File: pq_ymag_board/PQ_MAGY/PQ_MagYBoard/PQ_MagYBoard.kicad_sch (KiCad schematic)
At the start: 10 parts, among them J1 M20-7810245

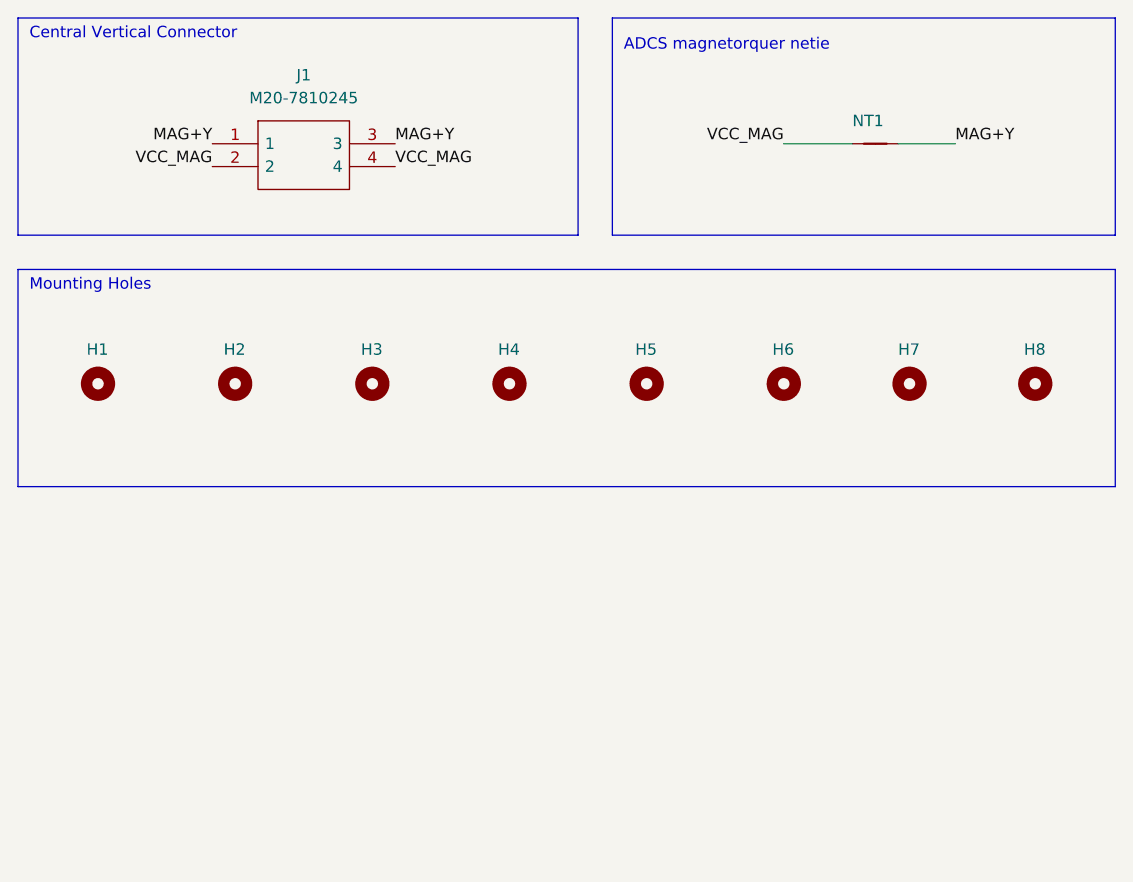
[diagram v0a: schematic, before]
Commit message: Full Kicad7 transition, library improvement and adaptation, correct footprints and 3D models added
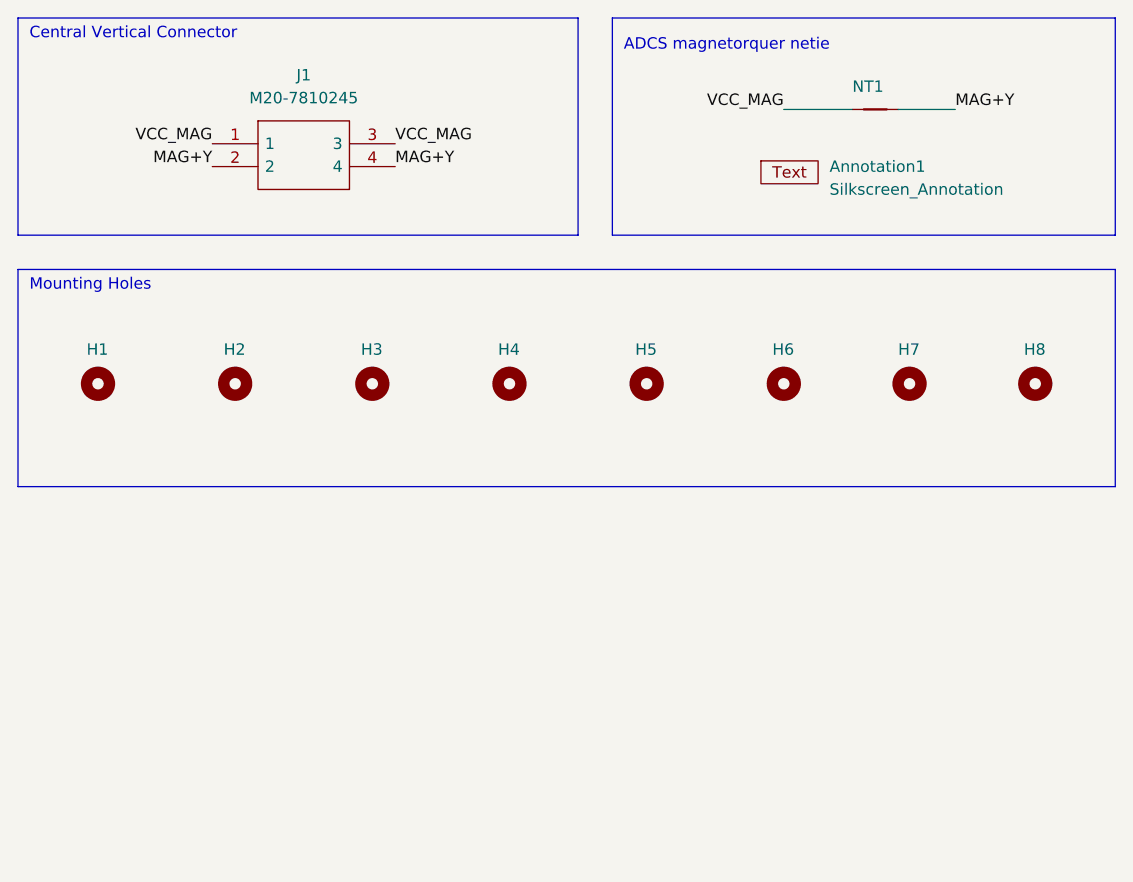
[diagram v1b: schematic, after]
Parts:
- added Annotation1: Silkscreen_Annotation, -nsl_symbols:Bridgemaker, symbol -nsl_symbols:Silkscreen_Annotation
- J1: footprint M207810245 -> -nsl_connector:M207810245
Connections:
- net MAG+Y: now also J1.2, J1.4; no longer J1.1, J1.3
- net VCC_MAG: now also J1.1, J1.3; no longer J1.2, J1.4
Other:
- moved on the sheet: NT1

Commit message: Small changes of component fields for the BOM
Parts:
- J1: Manufacturer 1 (none) -> Harwin; Manufacturer Part Number 1 (none) -> M20-7810245; Supplier 1 (none) -> Mouser; Supplier Part Number 1 (none) -> 855-M20-7810245
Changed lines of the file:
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@@
       (effects (font (size 1.27 1.27)) (justify left) hide)
+    )
+    (property "Manufacturer 1" "Harwin" (at 109.22 85.09 0)
+      (effects (font (size 1.27 1.27)) hide)
+    )
+    (property "Manufacturer Part Number 1" "M20-7810245" (at 109.22 85.09 0)
+      (effects (font (size 1.27 1.27)) hide)
+    )
+    (property "Supplier 1" "Mouser" (at 109.22 85.09 0)
+      (effects (font (size 1.27 1.27)) hide)
+    )
+    (property "Supplier Part Number 1" "855-M20-7810245" (at 109.22 85.09 0)
+      (effects (font (size 1.27 1.27)) hide)
     )
     (pin "1")

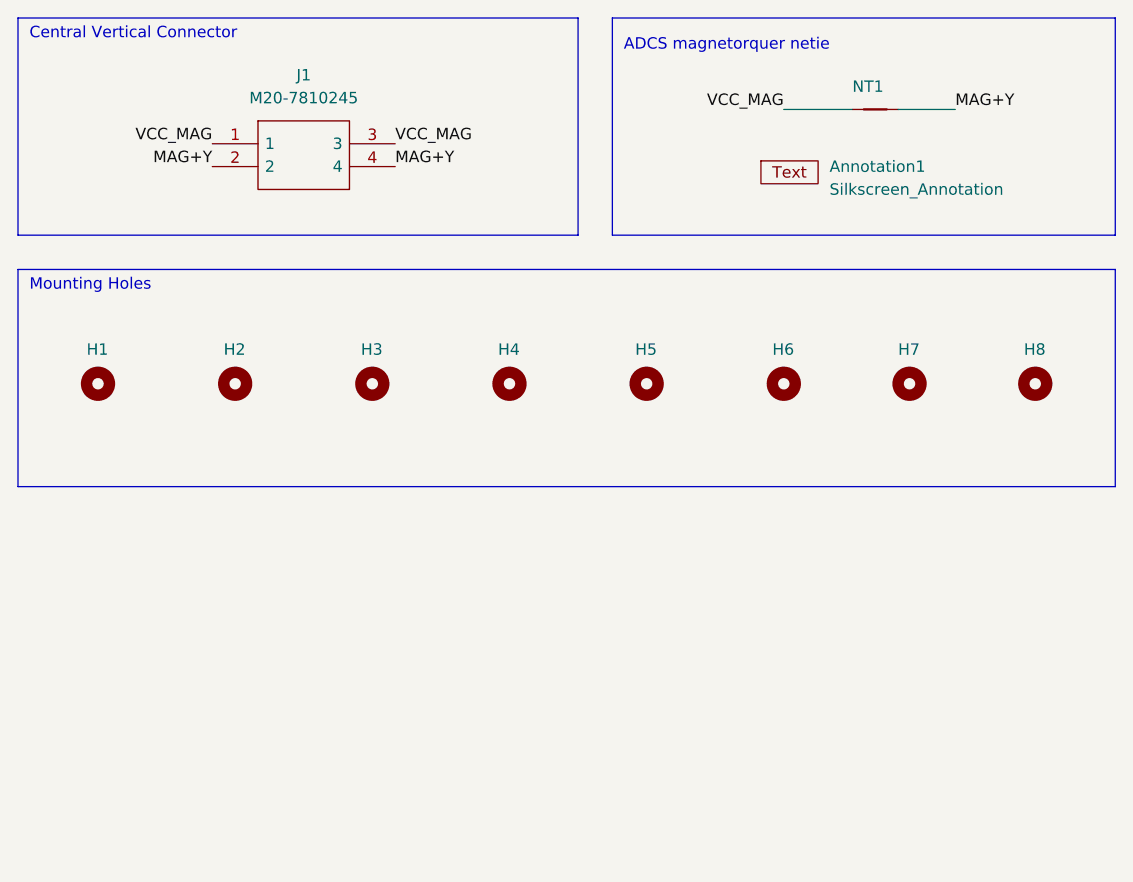
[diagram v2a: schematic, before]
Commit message: Add names of PQ collaborators in Y magnetorquer
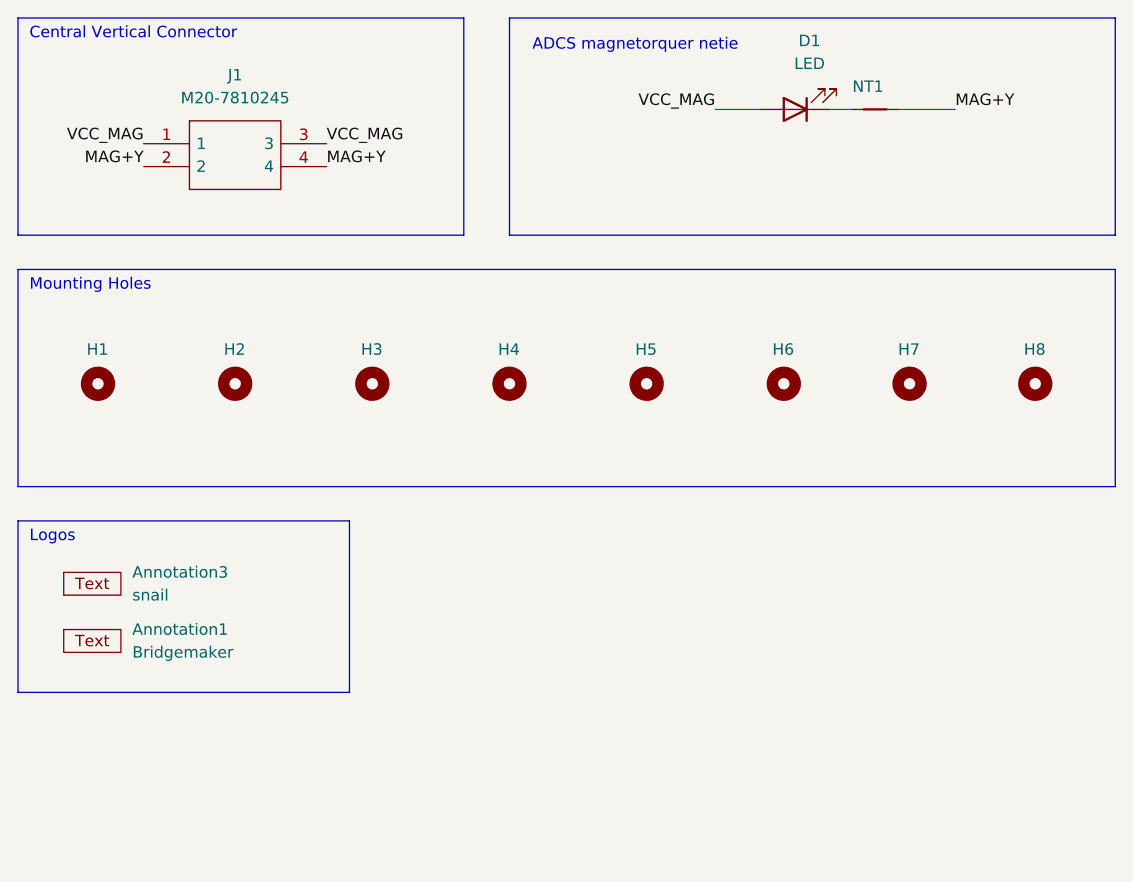
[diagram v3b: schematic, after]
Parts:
- added Annotation3: snail, snail:v2, symbol -nsl_symbols:Silkscreen_Annotation
- added D1: LED, LED_SMD:LED_0402_1005Metric, symbol Device:LED
- Annotation1: value Silkscreen_Annotation -> Bridgemaker
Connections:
- net VCC_MAG: now also D1.2 (A); no longer NT1.1
- new net: D1.1 (K), NT1.1
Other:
- note added: "Logos"
- moved on the sheet: Annotation1, J1

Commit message: Removed netie, reordered names, added diacritics, added NSL hexagonal logo
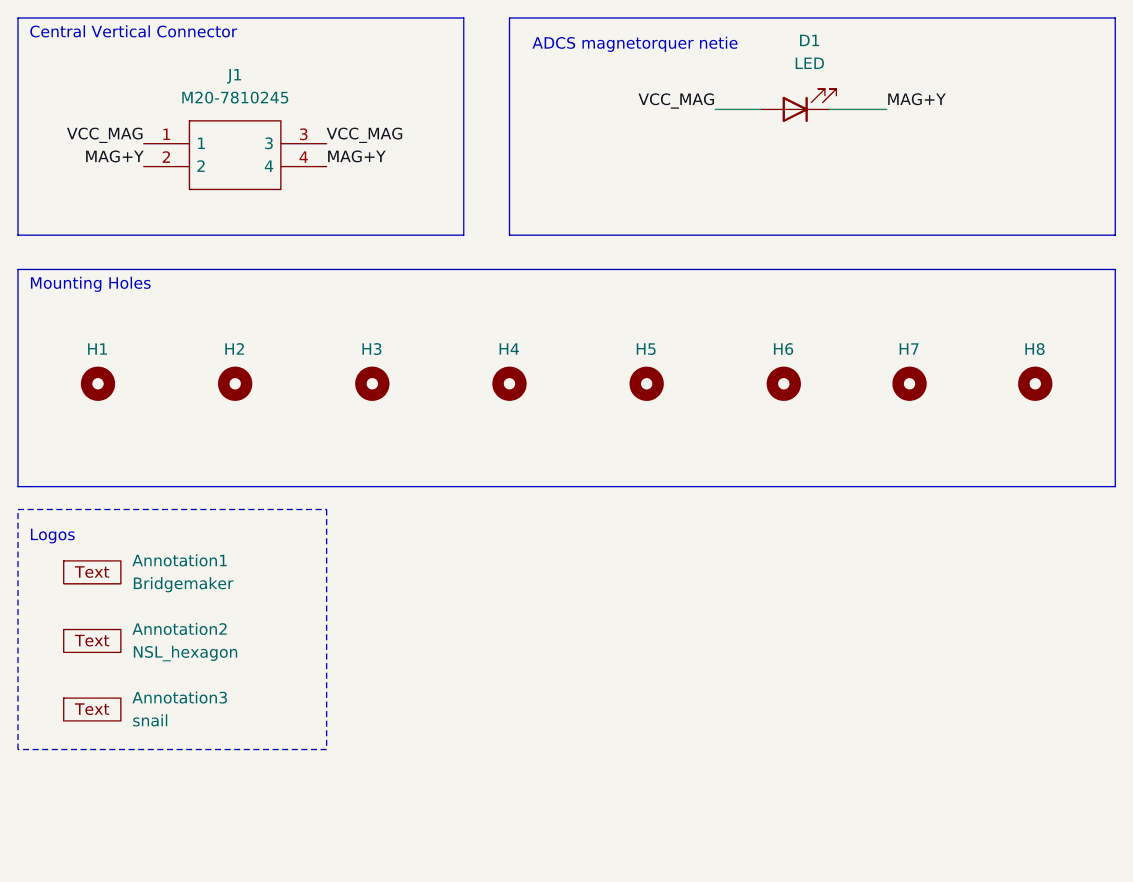
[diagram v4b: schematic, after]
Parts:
- removed NT1: NetTie_2, NetTie:NetTie-2_SMD_Pad0.5mm, symbol Device:NetTie_2
- added Annotation2: NSL_hexagon, symbols-nsl:NSL_hexagon, symbol symbols-nsl:Silkscreen_Annotation
- Annotation1: footprint -nsl_symbols:Bridgemaker -> symbols-nsl:Bridgemaker
- Annotation3: footprint snail:v2 -> symbols-nsl:Snail
- J1: footprint -nsl_connector:M207810245 -> connector-nsl:M207810245
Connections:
- net MAG+Y: now also D1.1 (K)
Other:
- moved on the sheet: Annotation1, Annotation3
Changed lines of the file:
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@@
-    (stroke (width 0) (type default))
-  )
-  (polyline (pts (xy 87.63 127) (xy 87.63 146.05))
-    (stroke (width 0) (type default))
-  )
-  (polyline (pts (xy 87.63 127) (xy 124.46 127))
     (stroke (width 0) (type default))
   )
@@
     (stroke (width 0) (type default))
   )
+  (wire (pts (xy 184.15 81.28) (xy 177.8 81.28))
+    (stroke (width 0) (type default))
+  )
   (polyline (pts (xy 87.63 71.12) (xy 87.63 95.25))
     (stroke (width 0) (type default))
@@
     (stroke (width 0) (type default))
   )
-  (wire (pts (xy 177.8 81.28) (xy 180.34 81.28))
-    (stroke (width 0) (type default))
-  )
   (polyline (pts (xy 142.24 95.25) (xy 209.55 95.25))
     (stroke (width 0) (type default))
@@
     (stroke (width 0) (type default))
   )
-  (wire (pts (xy 191.77 81.28) (xy 185.42 81.28))
-    (stroke (width 0.254) (type default))
-  )
-  (polyline (pts (xy 124.46 146.05) (xy 124.46 127))
-    (stroke (width 0) (type default))
-  )
   (polyline (pts (xy 209.55 71.12) (xy 209.55 95.25))
     (stroke (width 0) (type default))
   )
-  (polyline (pts (xy 87.63 146.05) (xy 124.46 146.05))
-    (stroke (width 0) (type default))
-  )
   (polyline (pts (xy 142.24 71.12) (xy 142.24 95.25))
     (stroke (width 0) (type default))
   )
+  (rectangle (start 87.63 125.73) (end 121.92 152.4)
+    (stroke (width 0) (type dash))
+    (fill (type none))
+  )
   (text "Logos" (at 88.9 129.54 0)
     (effects (font (size 1.27 1.27)) (justify left bottom))
@@
     (effects (font (size 1.27 1.27)) (justify left bottom))
   )
-  (label "MAG+Y" (at 191.77 81.28 0) (fields_autoplaced)
+  (label "MAG+Y" (at 184.15 81.28 0) (fields_autoplaced)
     (effects (font (size 1.27 1.27)) (justify left bottom))
   )
@@
     )
   )
-  (symbol (lib_id "-nsl_symbols:Silkscreen_Annotation") (at 93.98 139.7 0) (unit 1)
+  (symbol (lib_id "-nsl_symbols:Silkscreen_Annotation") (at 93.98 153.67 0) (unit 1)
     (in_bom yes) (on_board yes) (dnp no) (fields_autoplaced)
-    (property "Reference" "Annotation3" (at 100.33 132.715 0)
-      (effects (font (size 1.27 1.27)) (justify left))
-    )
-    (property "Value" "snail" (at 100.33 135.255 0)
-      (effects (font (size 1.27 1.27)) (justify left))
-    )
-    (property "Footprint" "snail:v2" (at 93.98 139.7 0)
-      (effects (font (size 1.27 1.27)) hide)
-    )
-    (property "Datasheet" "" (at 93.98 139.7 0)
+    (property "Reference" "Annotation3" (at 100.33 146.685 0)
+      (effects (font (size 1.27 1.27)) (justify left))
+    )
+    (property "Value" "snail" (at 100.33 149.225 0)
+      (effects (font (size 1.27 1.27)) (justify left))
+    )
+    (property "Footprint" "symbols-nsl:Snail" (at 93.98 153.67 0)
+      (effects (font (size 1.27 1.27)) hide)
+    )
+    (property "Datasheet" "" (at 93.98 153.67 0)
       (effects (font (size 1.27 1.27)) hide)
     )
@@
     )
   )
+  (symbol (lib_id "symbols-nsl:Silkscreen_Annotation") (at 93.98 146.05 0) (unit 1)
+    (in_bom yes) (on_board yes) (dnp no) (fields_autoplaced)
+    (property "Reference" "Annotation2" (at 100.33 139.065 0)
+      (effects (font (size 1.27 1.27)) (justify left))
+    )
+    (property "Value" "NSL_hexagon" (at 100.33 141.605 0)
+      (effects (font (size 1.27 1.27)) (justify left))
+    )
+    (property "Footprint" "symbols-nsl:NSL_hexagon" (at 93.98 146.05 0)
+      (effects (font (size 1.27 1.27)) hide)
+    )
+    (property "Datasheet" "" (at 93.98 146.05 0)
+      (effects (font (size 1.27 1.27)) hide)
+    )
+    (instances
+      (project "PQ_MagYBoard"
+        (path "/69ef6fcb-01e8-4c0b-998b-22cdfd5dc558"
+          (reference "Annotation2") (unit 1)
+        )
+      )
+    )
+  )
   (symbol (lib_id "Mechanical:MountingHole") (at 111.76 111.76 0) (unit 1)
     (in_bom yes) (on_board yes) (dnp no)
@@
     )
   )
-  (symbol (lib_id "-nsl_symbols:Silkscreen_Annotation") (at 93.98 146.05 0) (unit 1)
+  (symbol (lib_id "-nsl_symbols:Silkscreen_Annotation") (at 93.98 138.43 0) (unit 1)
     (in_bom yes) (on_board yes) (dnp no) (fields_autoplaced)
-    (property "Reference" "Annotation1" (at 100.33 139.065 0)
-      (effects (font (size 1.27 1.27)) (justify left))
-    )
-    (property "Value" "Bridgemaker" (at 100.33 141.605 0)
-      (effects (font (size 1.27 1.27)) (justify left))
-    )
-    (property "Footprint" "-nsl_symbols:Bridgemaker" (at 93.98 146.05 0)
-      (effects (font (size 1.27 1.27)) hide)
-    )
-    (property "Datasheet" "" (at 93.98 146.05 0)
+    (property "Reference" "Annotation1" (at 100.33 131.445 0)
+      (effects (font (size 1.27 1.27)) (justify left))
+    )
+    (property "Value" "Bridgemaker" (at 100.33 133.985 0)
+      (effects (font (size 1.27 1.27)) (justify left))
+    )
+    (property "Footprint" "symbols-nsl:Bridgemaker" (at 93.98 138.43 0)
+      (effects (font (size 1.27 1.27)) hide)
+    )
+    (property "Datasheet" "" (at 93.98 138.43 0)
       (effects (font (size 1.27 1.27)) hide)
     )
@@
       (effects (font (size 1.27 1.27)))
     )
-    (property "Footprint" "-nsl_connector:M207810245" (at 118.11 82.55 0)
+    (property "Footprint" "connector-nsl:M207810245" (at 118.11 82.55 0)
       (effects (font (size 1.27 1.27)) (justify left) hide)
     )
@@
         )
       )
-    )
-  )
-  (symbol (lib_id "Device:NetTie_2") (at 182.88 81.28 0) (unit 1)
-    (in_bom yes) (on_board yes) (dnp no)
-    (property "Reference" "NT1" (at 180.34 78.74 0)
-      (effects (font (size 1.27 1.27)) (justify left))
-    )
-    (property "Value" "NetTie_2" (at 184.15 81.28 90)
-      (effects (font (size 1.27 1.27)) (justify left) hide)
-    )
-    (property "Footprint" "NetTie:NetTie-2_SMD_Pad0.5mm" (at 182.88 81.28 0)
-      (effects (font (size 1.27 1.27)) hide)
-    )
-    (property "Datasheet" "~" (at 182.88 81.28 0)
-      (effects (font (size 1.27 1.27)) hide)
-    )
-    (pin "1")
-    (pin "2")
-    (instances
-      (project "PQ_MagYBoard"
-        (path "/69ef6fcb-01e8-4c0b-998b-22cdfd5dc558"
-          (reference "NT1") (unit 1)
-        )
-      )

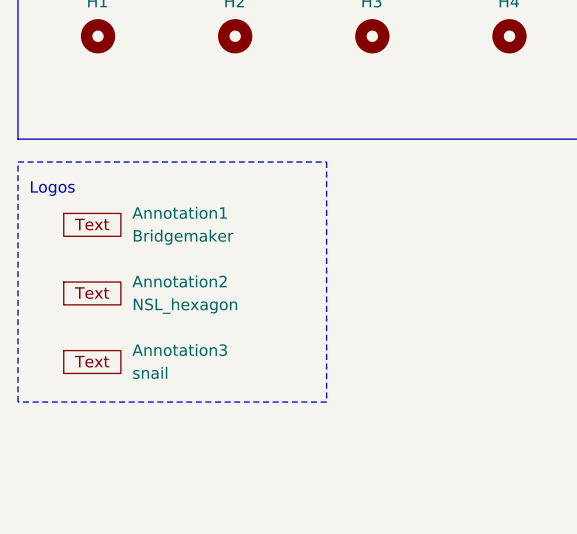
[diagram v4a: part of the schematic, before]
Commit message: add more names
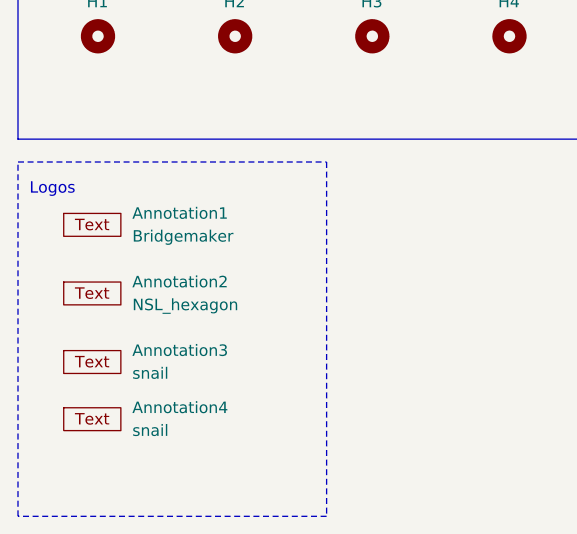
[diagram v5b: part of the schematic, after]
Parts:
- added Annotation4: snail, symbols-nsl:pocat_lektron, symbol -nsl_symbols:Silkscreen_Annotation
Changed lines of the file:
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@@
     (stroke (width 0) (type default))
   )
-  (rectangle (start 87.63 125.73) (end 121.92 152.4)
+  (rectangle (start 87.63 125.73) (end 121.92 165.1)
     (stroke (width 0) (type dash))
     (fill (type none))
@@
         )
       )
+    )
+  )
+  (symbol (lib_id "-nsl_symbols:Silkscreen_Annotation") (at 93.98 160.02 0) (unit 1)
+    (in_bom yes) (on_board yes) (dnp no) (fields_autoplaced)
+    (property "Reference" "Annotation4" (at 100.33 153.035 0)
+      (effects (font (size 1.27 1.27)) (justify left))
+    )
+    (property "Value" "snail" (at 100.33 155.575 0)
+      (effects (font (size 1.27 1.27)) (justify left))
+    )
+    (property "Footprint" "symbols-nsl:pocat_lektron" (at 93.98 160.02 0)
+      (effects (font (size 1.27 1.27)) hide)
+    )
+    (property "Datasheet" "" (at 93.98 160.02 0)
+      (effects (font (size 1.27 1.27)) hide)
+    )
+    (instances
+      (project "PQ_MagYBoard"
+        (path "/69ef6fcb-01e8-4c0b-998b-22cdfd5dc558"
+          (reference "Annotation4") (unit 1)
+        )
+      )
